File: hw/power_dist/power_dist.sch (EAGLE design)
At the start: 57 parts, among them J1 JST-ZH6SMT_VERT, J2 JST-PH4SMT_VERT, P1 XT30P, P2 XT30P, P3 XT30P, P4 XT30P, P5 XT30P, P6 XT30P, P7 XT90PW-M, Q1 TPH1R204PL, Q2 TPH1R204PL, Q3 TPH1R204PL, U1 ZXTR2012Z, U2 MAX150628TDFN, U3 STM32G474CEU6, U4 MIC4416, U5 MIC4416, U6 TCAN334G

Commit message: r3 of power_dist
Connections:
- net LED1: now also U3.PB9; no longer U3.PC15-OSC32_OUT
- net LED2: now also U3.PB7; no longer U3.PC14-OSC32_IN
- net SWCLK: now also U3.PA14; no longer U3.PA15
- net SWDIO: now also U3.PA13; no longer U3.PA14
- net VCC: now also U3.VBAT
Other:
- note added: "moteus power dist r3 (c) 2019 Josh Pieper, jjp@pobox.com Licensed under the Apache 2.0 License https://www.apache.org/licenses/LICENSE-2.0"
- note removed: "moteus power dist (c) 2019 Josh Pieper, jjp@pobox.com Licensed under the Apache 2.0 License https://www.apache.org/licenses/LICENSE-2.0"
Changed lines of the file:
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@@
 </part>
 <part name="P+20" library="supply1" deviceset="+18V" device=""/>
+<part name="P+21" library="supply1" deviceset="VCC" device=""/>
 </parts>
 <sheets>
 <sheet>
 <plain>
-<text x="-78.74" y="218.44" size="5.08" layer="91">moteus power dist
+<text x="-78.74" y="218.44" size="5.08" layer="91">moteus power dist r3
 (c) 2019 Josh Pieper, jjp@pobox.com
 Licensed under the Apache 2.0 License
@@
 </instance>
 <instance part="P+20" gate="1" x="284.48" y="17.78"/>
+<instance part="P+21" gate="VCC" x="441.96" y="157.48"/>
 </instances>
 <busses>
@@
 <wire x1="287.02" y1="-22.86" x2="299.72" y2="-22.86" width="0.1524" layer="91"/>
 </segment>
+<segment>
+<pinref part="P+21" gate="VCC" pin="VCC"/>
+<wire x1="441.96" y1="154.94" x2="441.96" y2="152.4" width="0.1524" layer="91"/>
+<pinref part="U3" gate="G$1" pin="VBAT"/>
+<wire x1="441.96" y1="152.4" x2="447.04" y2="152.4" width="0.1524" layer="91"/>
+</segment>
 </net>
 <net name="N$1" class="0">
@@
 </segment>
 <segment>
-<pinref part="U3" gate="G$1" pin="PA14"/>
-<wire x1="485.14" y1="175.26" x2="485.14" y2="203.2" width="0.1524" layer="91"/>
-<label x="485.14" y="198.12" size="1.778" layer="95" font="vector" rot="R90"/>
+<pinref part="U3" gate="G$1" pin="PA13"/>
+<wire x1="492.76" y1="152.4" x2="497.84" y2="152.4" width="0.1524" layer="91"/>
+<wire x1="497.84" y1="152.4" x2="497.84" y2="198.12" width="0.1524" layer="91"/>
+<label x="497.84" y="190.5" size="1.778" layer="95" rot="R90"/>
 </segment>
 </net>
@@
 </segment>
 <segment>
-<pinref part="U3" gate="G$1" pin="PA15"/>
-<wire x1="482.6" y1="175.26" x2="482.6" y2="203.2" width="0.1524" layer="91"/>
-<label x="482.6" y="198.12" size="1.778" layer="95" font="vector" rot="R90"/>
+<pinref part="U3" gate="G$1" pin="PA14"/>
+<wire x1="485.14" y1="175.26" x2="485.14" y2="198.12" width="0.1524" layer="91"/>
+<label x="485.14" y="190.5" size="1.778" layer="95" rot="R90"/>
 </segment>
 </net>
@@
 </segment>
 <segment>
-<pinref part="U3" gate="G$1" pin="PC15-OSC32_OUT"/>
-<wire x1="447.04" y1="144.78" x2="424.18" y2="144.78" width="0.1524" layer="91"/>
-<label x="424.18" y="144.78" size="1.778" layer="95" font="vector"/>
+<pinref part="U3" gate="G$1" pin="PB9"/>
+<wire x1="459.74" y1="175.26" x2="459.74" y2="187.96" width="0.1524" layer="91"/>
+<label x="459.74" y="182.88" size="1.778" layer="95" rot="R90"/>
 </segment>
 </net>
@@
 </segment>
 <segment>
-<pinref part="U3" gate="G$1" pin="PC14-OSC32_IN"/>
-<wire x1="447.04" y1="147.32" x2="424.18" y2="147.32" width="0.1524" layer="91"/>
-<label x="424.18" y="147.32" size="1.778" layer="95" font="vector"/>
-</segment>
-</net>
+<pinref part="U3" gate="G$1" pin="PB7"/>
+<wire x1="464.82" y1="175.26" x2="464.82" y2="187.96" width="0.1524" layer="91"/>
+<label x="464.82" y="182.88" size="1.778" layer="95" rot="R90"/>
+</segment>
+</net>

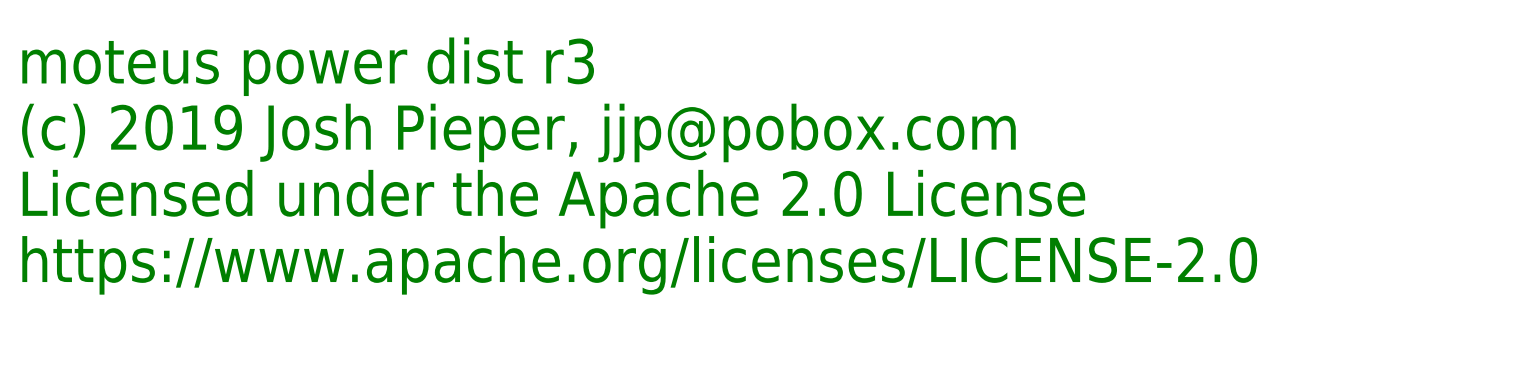
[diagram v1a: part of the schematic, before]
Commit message: Add mjbots logo to power dist board
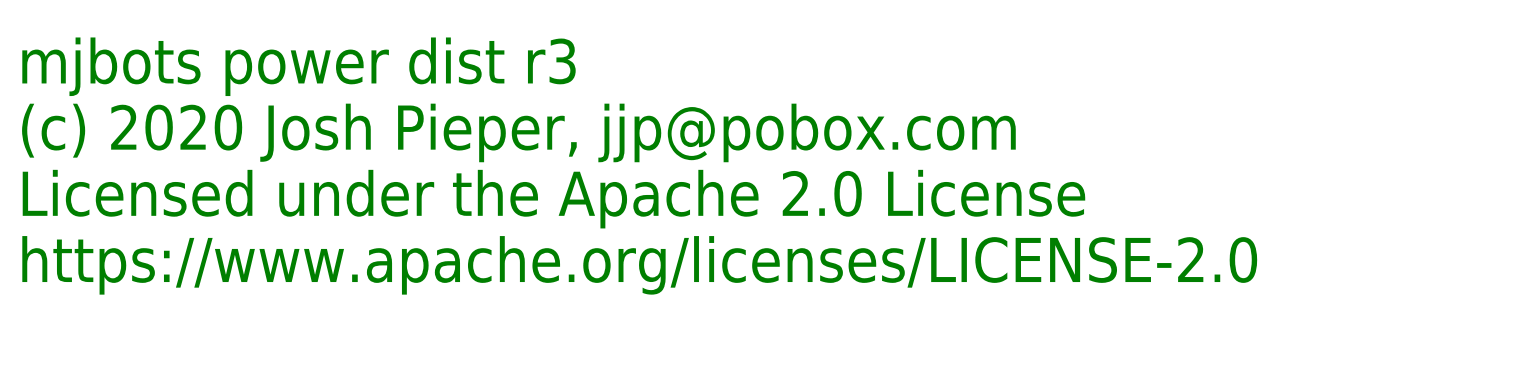
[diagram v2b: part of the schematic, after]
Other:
- note added: "mjbots power dist r3 (c) 2020 Josh Pieper, jjp@pobox.com Licensed under the Apache 2.0 License https://www.apache.org/licenses/LICENSE-2.0"
- note removed: "moteus power dist r3 (c) 2019 Josh Pieper, jjp@pobox.com Licensed under the Apache 2.0 License https://www.apache.org/licenses/LICENSE-2.0"
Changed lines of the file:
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@@
 <sheet>
 <plain>
-<text x="-78.74" y="218.44" size="5.08" layer="91">moteus power dist r3
-(c) 2019 Josh Pieper, jjp@pobox.com
+<text x="-78.74" y="218.44" size="5.08" layer="91">mjbots power dist r3
+(c) 2020 Josh Pieper, jjp@pobox.com
 Licensed under the Apache 2.0 License
 https://www.apache.org/licenses/LICENSE-2.0</text>

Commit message: Update power dist to 3.1
The only change is switching out the CAN transceiver for the LTC2875
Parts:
- U6: MF TI -> Analog; MPN TCAN334GDR -> LTC2875IS8
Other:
- note added: "mjbots power dist r3.1 (c) 2020 Josh Pieper, jjp@pobox.com Licensed under the Apache 2.0 License https://www.apache.org/licenses/LICENSE-2.0"
- note removed: "mjbots power dist r3 (c) 2020 Josh Pieper, jjp@pobox.com Licensed under the Apache 2.0 License https://www.apache.org/licenses/LICENSE-2.0"

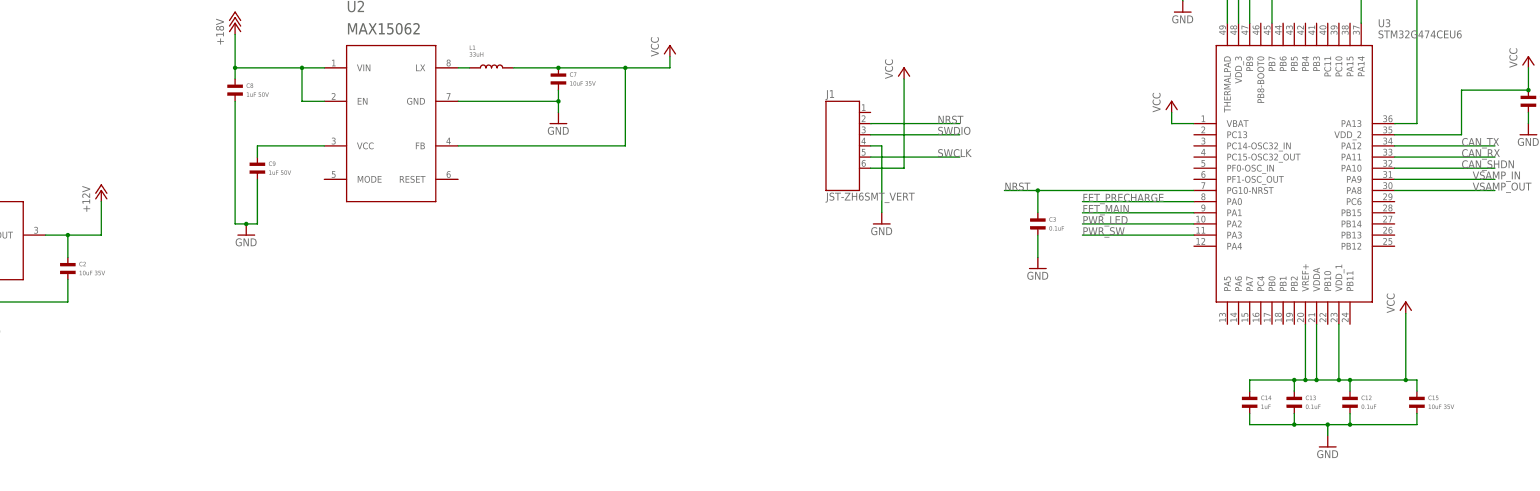
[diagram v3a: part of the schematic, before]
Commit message: Switch capacitors to soft termination variant
Round corners
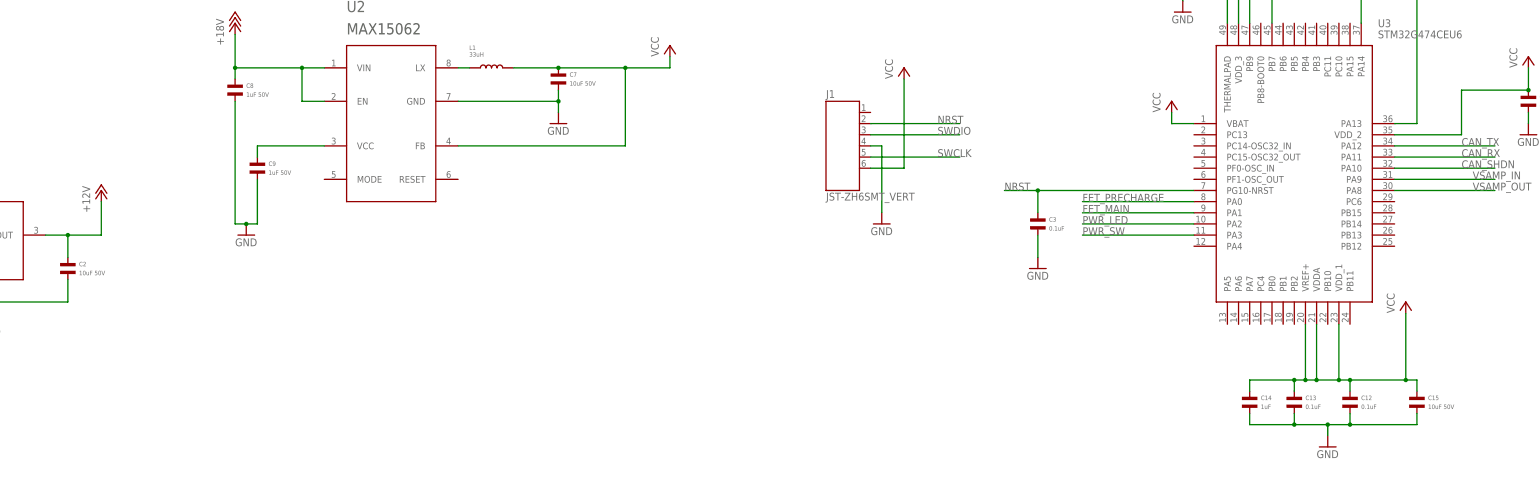
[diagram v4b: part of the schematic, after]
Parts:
- C15, C2, C7: value 10uF 35V -> 10uF 50V; MPN CGA5L1X7R1V106K160AC -> C3216X7R1H106K160AE
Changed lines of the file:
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@@
 <part name="P+4" library="supply1" deviceset="+18V" device=""/>
 <part name="P+5" library="supply1" deviceset="+12V" device=""/>
-<part name="C2" library="mfpassives" deviceset="CAPACITOR_NP" device="_1206" value="10uF 35V">
+<part name="C2" library="mfpassives" deviceset="CAPACITOR_NP" device="_1206" value="10uF 50V">
 <attribute name="MF" value="TDK"/>
-<attribute name="MPN" value="CGA5L1X7R1V106K160AC"/>
+<attribute name="MPN" value="C3216X7R1H106K160AE"/>
 </part>
 <part name="P+3" library="supply1" deviceset="+12V" device=""/>
@@
 <attribute name="POPULATE" value="1"/>
 </part>
-<part name="C7" library="mfpassives" deviceset="CAPACITOR_NP" device="_1206" value="10uF 35V">
+<part name="C7" library="mfpassives" deviceset="CAPACITOR_NP" device="_1206" value="10uF 50V">
 <attribute name="MF" value="TDK"/>
-<attribute name="MPN" value="CGA5L1X7R1V106K160AC"/>
+<attribute name="MPN" value="C3216X7R1H106K160AE"/>
 </part>
 <part name="C8" library="mfpassives" deviceset="CAPACITOR_NP" device="_0603" value="1uF 50V">
@@
 <attribute name="MPN" value="MF-CAP-0402-1uF"/>
 </part>
-<part name="C15" library="mfpassives" deviceset="CAPACITOR_NP" device="_1206" value="10uF 35V">
+<part name="C15" library="mfpassives" deviceset="CAPACITOR_NP" device="_1206" value="10uF 50V">
 <attribute name="MF" value="TDK"/>
-<attribute name="MPN" value="CGA5L1X7R1V106K160AC"/>
+<attribute name="MPN" value="C3216X7R1H106K160AE"/>
 </part>
 <part name="J1" library="precharge" deviceset="JST-ZH6" device="SMT_VERT">
